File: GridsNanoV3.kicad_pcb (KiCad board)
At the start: 2 copper layers, 164.6 x 108 mm, 112 parts, among them J10 Conn_01x12, J11 Conn_01x12, J12 Conn_02x05_Odd_Even, J13 Conn_01x10, J14 Conn_01x10, J15 Conn_01x10, J16 Conn_01x03, J7 Conn_01x10, Q1 2N3904, Q2 2N3904, U1 MCP6002_1, U2 MCP6002_1, U3 MCP6002_1, U4 L7805, U5 LM4040LP-5, U6 74HC595, X1 CV_X, Y1 CV_Y

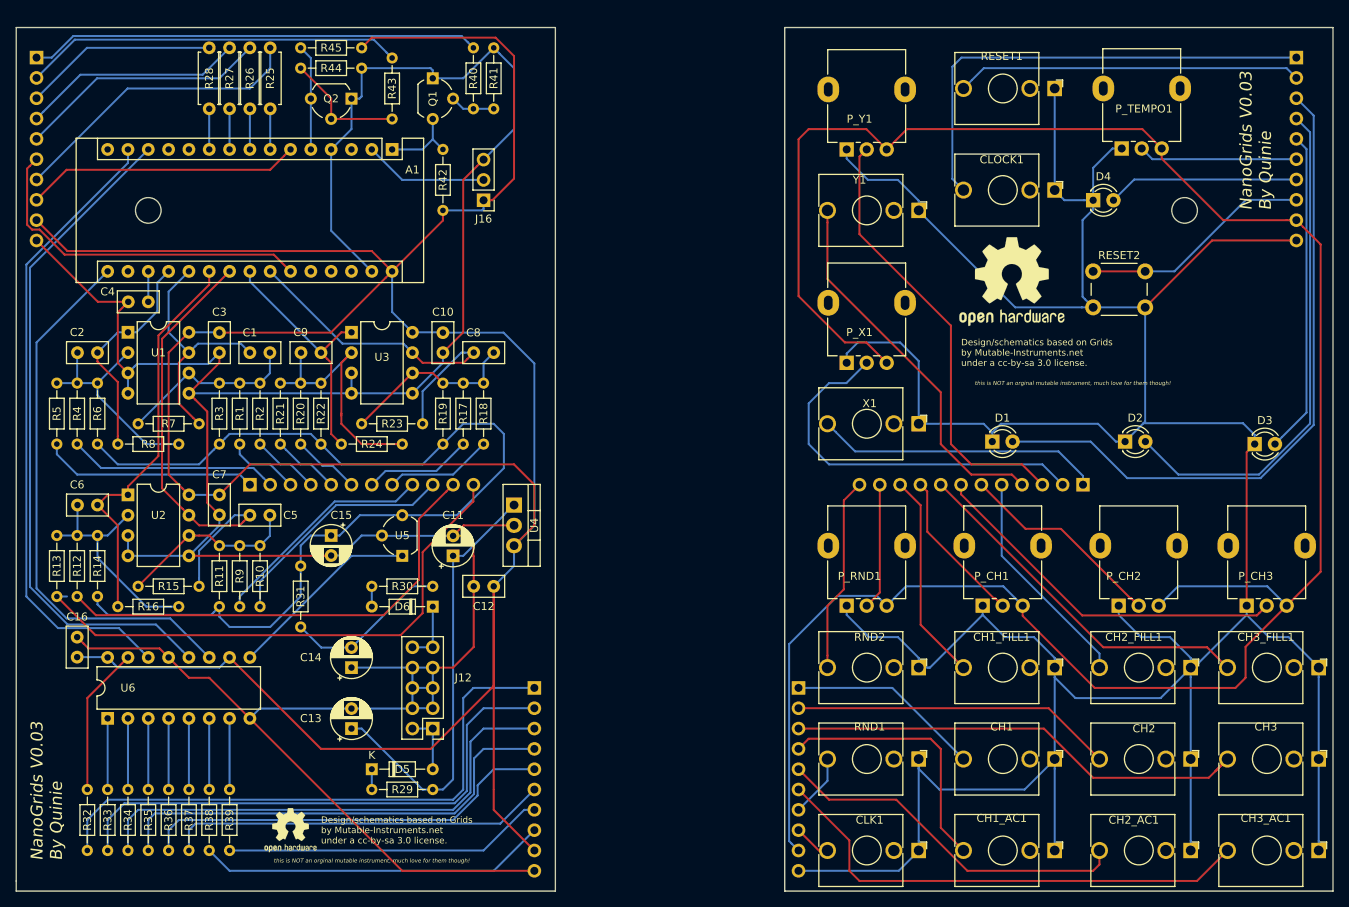
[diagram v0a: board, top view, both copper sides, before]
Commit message: Updates 0.04
Updates for 0.04
Change footprint for pots
Added + sign for leds
Added usb side
Added Ground plane
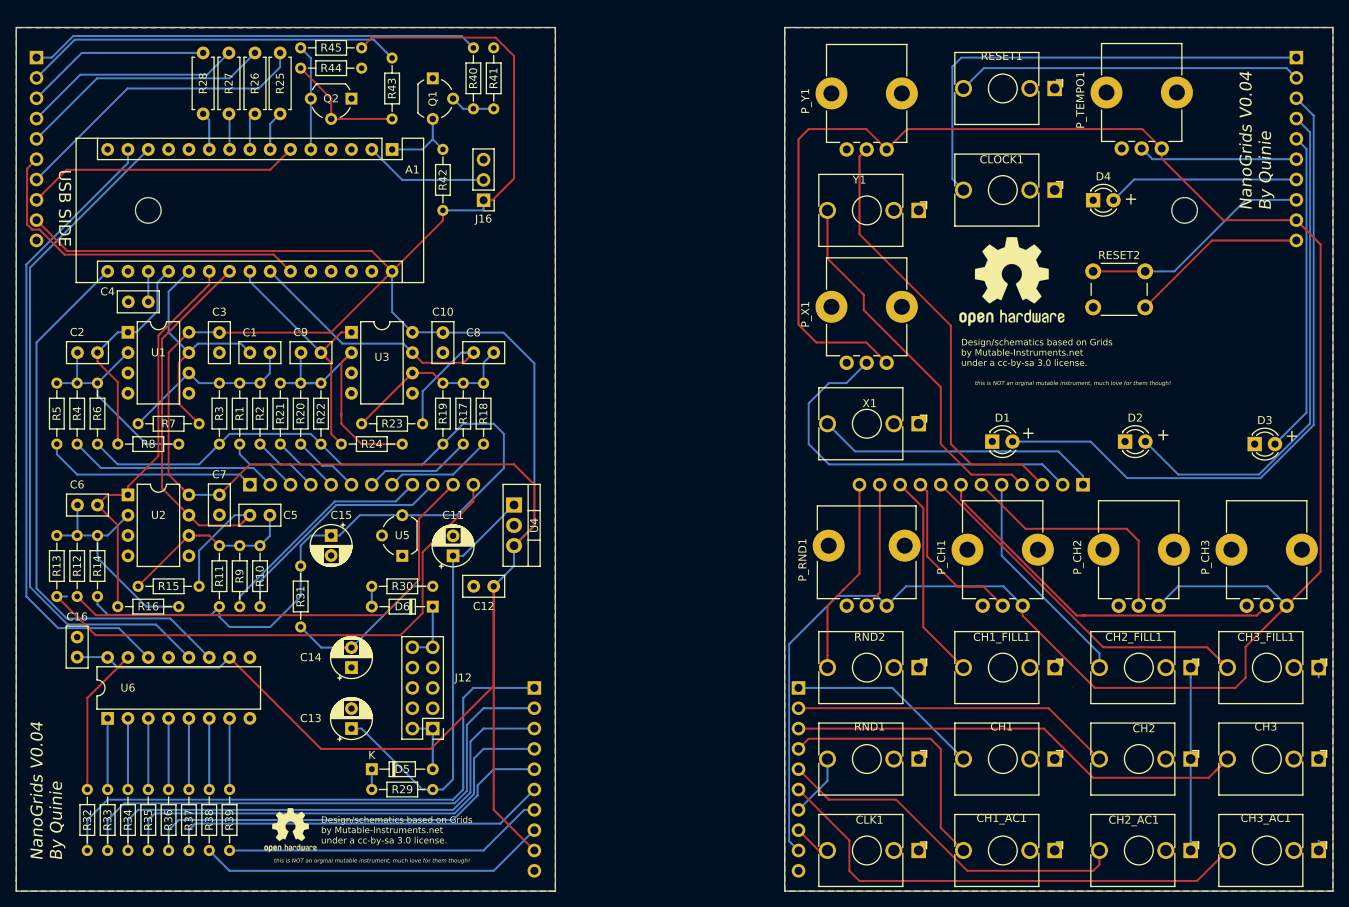
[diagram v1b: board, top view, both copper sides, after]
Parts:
- C15: value 0.47nf -> 0.47uf
- D5, D6: value D -> 1n4148
- P_CH1, P_CH2, P_CH3, P_TEMPO1, P_X1, P_Y1: footprint Potentiometer_THT:Potentiometer_Alpha_RD901F-40-00D_Single_Vertical -> Potentiometer_THT:Potentiometer_Alps_RK09K_Single_Vertical
- P_RND1: footprint Potentiometer_THT:Potentiometer_Alpha_RD901F-40-00D_Single_Vertical -> Potentiometer_THT:Potentiometer_Alps_RK09L_Single_Vertical
- moved P_CH3 5.00 mm to (260.4, 90.0)
- moved P_CH1 5.00 mm to (227.4, 90.0)
- moved P_CH2 5.00 mm to (244.4, 90.0)
- moved P_RND1 5.00 mm to (210.4, 90.0)
- moved P_TEMPO1 5.00 mm to (244.8, 32.9)
- moved P_X1 5.00 mm to (210.4, 59.7)
- moved P_Y1 5.00 mm to (210.4, 33.0)
- moved R25 1.40 mm to (134.6, 28.6)
- moved R28 0.99 mm to (125.0, 28.6)
- moved R26 0.90 mm to (131.4, 28.6)
- moved R27 0.64 mm to (128.2, 28.6)
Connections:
- P_CH1 pad 1: GND -> +5V
- P_CH1 pad 3: +5V -> GND
- P_CH2 pad 1: GND -> +5V
- P_CH2 pad 3: +5V -> GND
- P_CH3 pad 1: GND -> +5V
- P_CH3 pad 3: +5V -> GND
- P_RND1 pad 1: GND -> +5V
- P_RND1 pad 3: +5V -> GND
- P_TEMPO1 pad 1: GND -> +5V
- P_TEMPO1 pad 3: +5V -> GND
- P_X1 pad 1: GND -> +5V
- P_X1 pad 3: +5V -> GND
- P_Y1 pad 1: GND -> +5V
- P_Y1 pad 3: +5V -> GND
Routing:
- net GND: track 812.1 -> 48.5 mm
- net (no net): track 24.3 -> 0.00 mm
- net P_CH2: track 34.4 -> 39.1 mm
- net +5V: track 652.7 -> 654.8 mm
- net P_CH1: track 48.1 -> 50.0 mm
- net LED_CH1: track 108.2 -> 107.2 mm
- net P_CH3: track 59.7 -> 60.5 mm
- net Net-(A1-Pad9): track 5.08 -> 4.48 mm
- net LED_CLOCK: track 61.4 -> 62.0 mm
- added copper zone on B.Cu, net GND
- added copper zone on F.Cu, net GND
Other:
- board text added: "+"
- board text added: "NanoGrids V0.04 By Quinie"
- board text added: "USB SIDE"
- board text removed: "NanoGrids V0.03 By Quinie"

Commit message: Gerber Update
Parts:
- moved D6 14.0 mm to (139.8, 89.2), turned to 0 degrees
- moved D5 3.50 mm to (143.6, 113.0), turned to 180 degrees
- moved R30 1.52 mm to (147.3, 86.8), turned to 180 degrees
- moved J12 0.61 mm to (154.3, 105.5)
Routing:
- net Net-(D5-Pad2): track 7.62 -> 23.5 mm
- net +5V: track 654.8 -> 670.4 mm
- net Net-(D6-Pad1): track 7.62 -> 17.1 mm
- net -12V: track 20.8 -> 15.1 mm
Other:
- board text added: "NanoGrids V0.041 By Quinie"
- board text removed: "NanoGrids V0.04 By Quinie"
